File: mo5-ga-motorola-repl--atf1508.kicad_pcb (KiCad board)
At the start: 2 copper layers, 15 parts, among them J1 JTAG, J2 GATE_ARRAY_MO5_V1_SOCKET, J3 VPP, U1 ATF1508AS_L_100A_TQFP_JTAG_EN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

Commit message: pcb : adjusting
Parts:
- moved C8 30.0 mm to (132.5, 119.7)
- moved C1 6.98 mm to (97.5, 119.4), turned to 0 degrees
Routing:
- net GND: track 2.92 -> 21.1 mm, vias 0 -> 1
- net +5V: track 0.00 -> 2.43 mm, vias 0 -> 1
- net /CPLD/TDI: track 8.51 -> 7.91 mm
- added copper zone on B.Cu, net GND
- added copper zone on F.Cu, net GND
- added copper zone on In1.Cu, net GND
- added copper zone on In2.Cu, net GND
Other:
- copper layers 2 -> 4

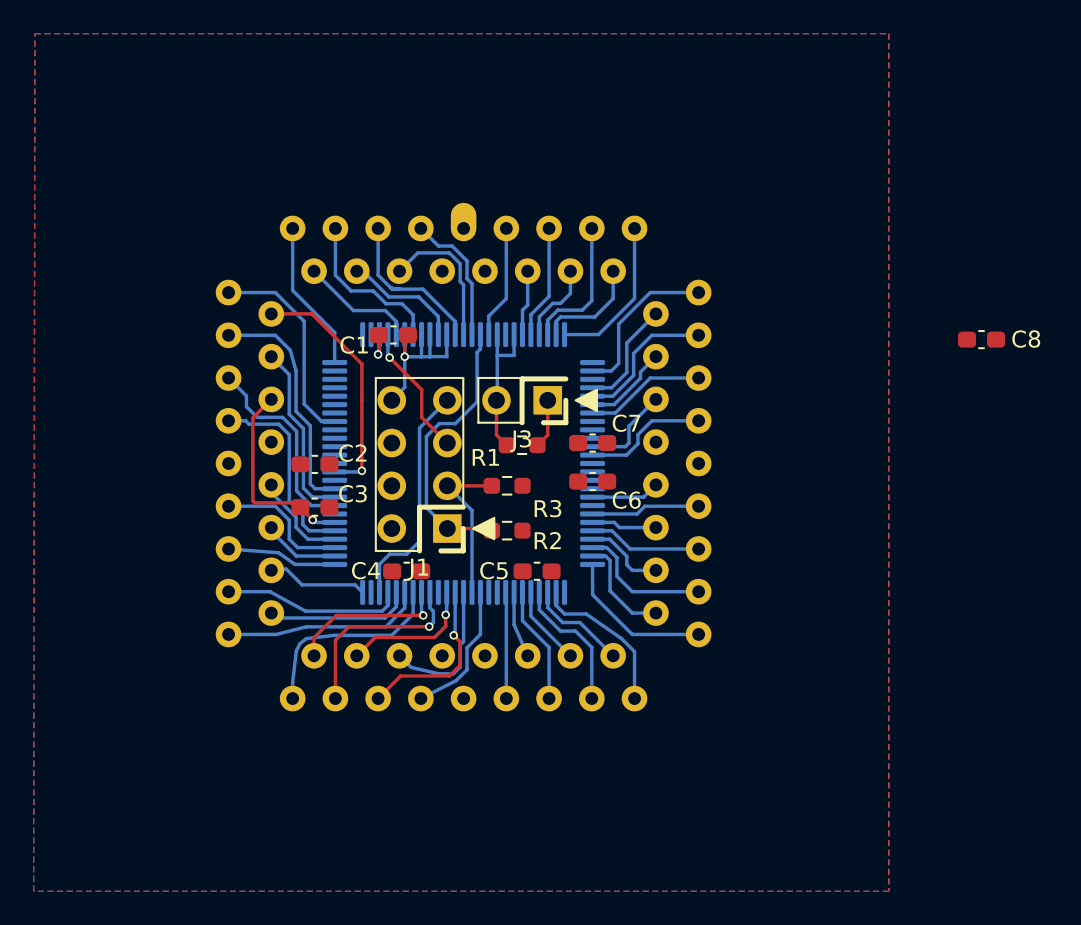
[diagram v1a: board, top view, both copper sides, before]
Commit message: pcb : slowly adjusting traces
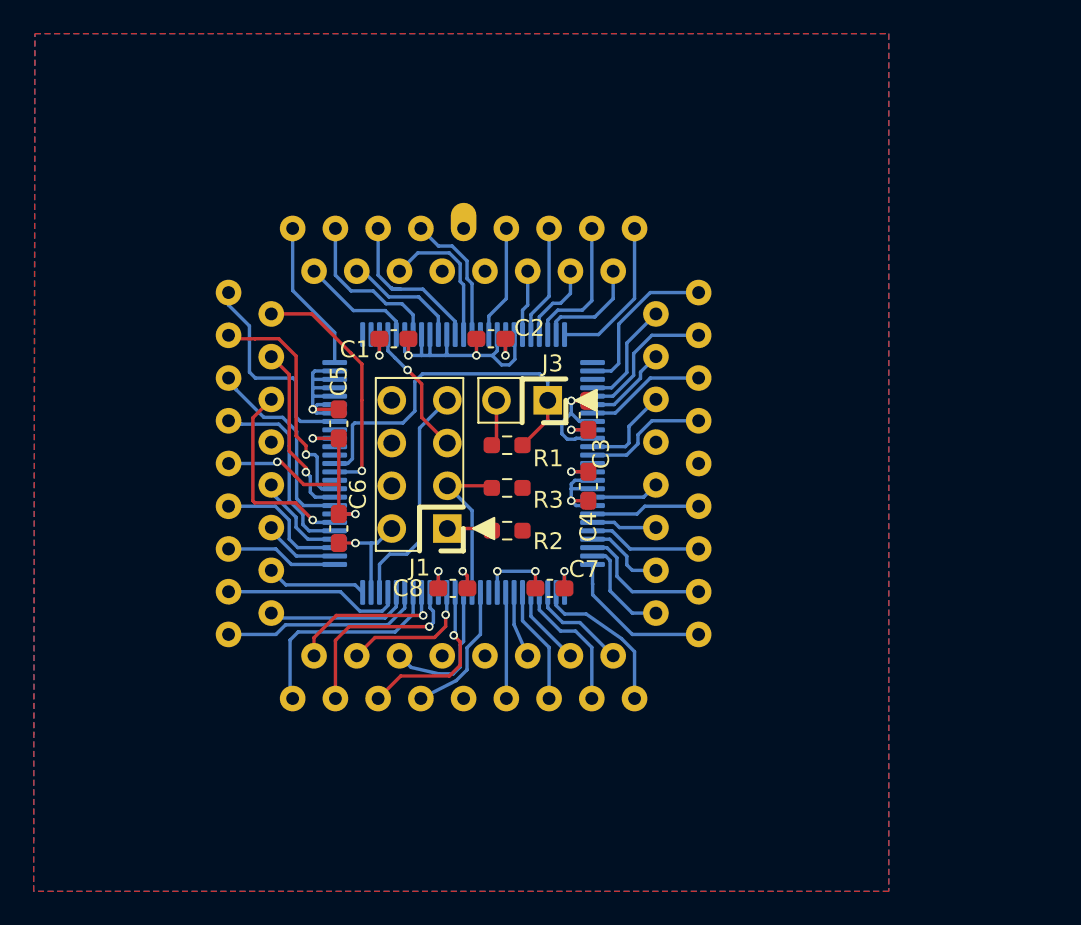
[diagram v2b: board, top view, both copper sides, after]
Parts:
- moved C8 34.7 mm to (101.0, 134.5), turned to 180 degrees
- moved C3 17.1 mm to (109.1, 124.2), turned to -90 degrees
- moved C6 15.3 mm to (94.3, 130.9), turned to -90 degrees
- moved C5 14.7 mm to (94.3, 124.7), turned to 90 degrees
- moved C2 12.9 mm to (103.3, 119.7)
- moved C4 11.9 mm to (109.1, 128.4), turned to 90 degrees
- moved C7 9.00 mm to (106.8, 134.5)
- moved R1 0.89 mm to (104.3, 126.0)
- moved C1 0.23 mm to (97.5, 119.7)
- moved R3 0.13 mm to (104.3, 128.5)
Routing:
- net GND: track 21.1 -> 56.3 mm, vias 1 -> 9
- net +5V: track 2.43 -> 30.3 mm, vias 1 -> 9
- net /CPLD/VPP: track 2.92 -> 21.7 mm
- net /CPLD/TMS: track 16.6 -> 2.70 mm
- net CLOCK: track 12.0 -> 12.8 mm
- net ~{CKLP}: track 13.9 -> 14.1 mm, vias 0 -> 1
- net SYCL: track 10.7 -> 10.6 mm, vias 0 -> 1

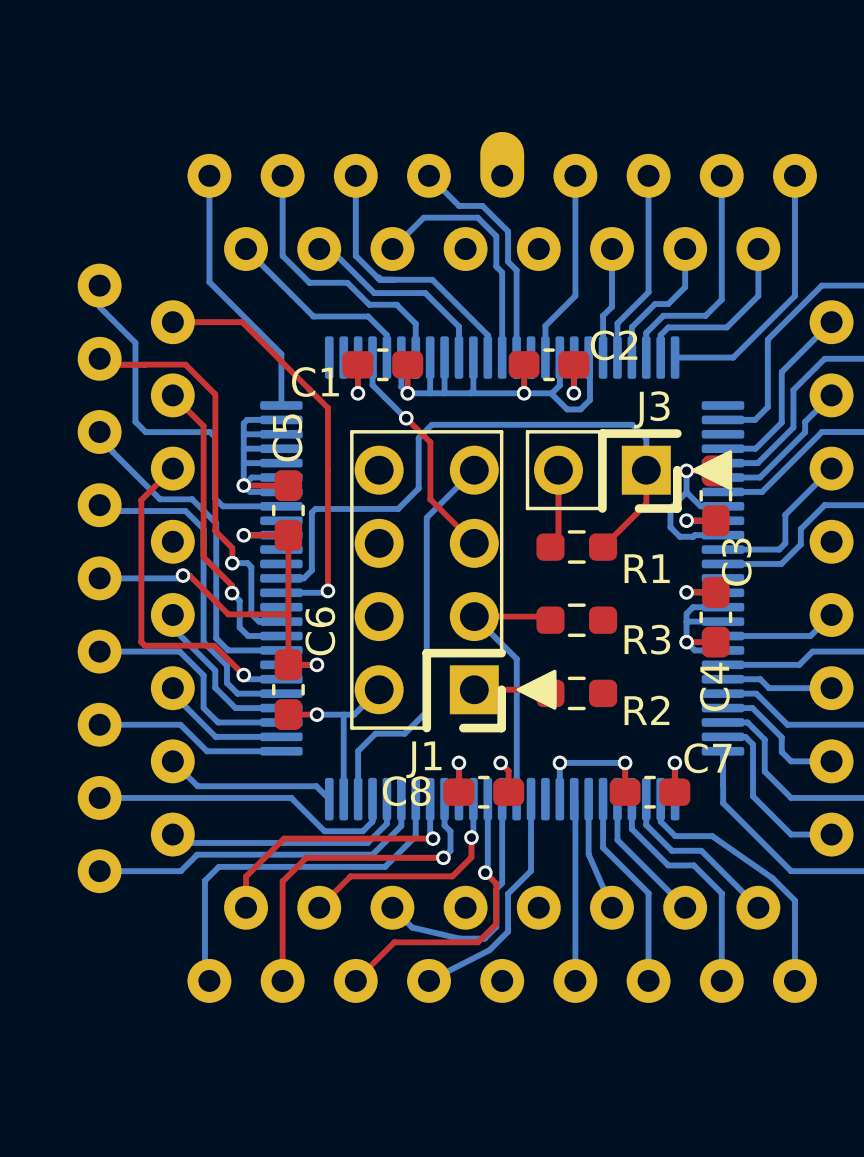
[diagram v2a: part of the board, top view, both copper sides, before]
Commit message: pcb : adjusting traces
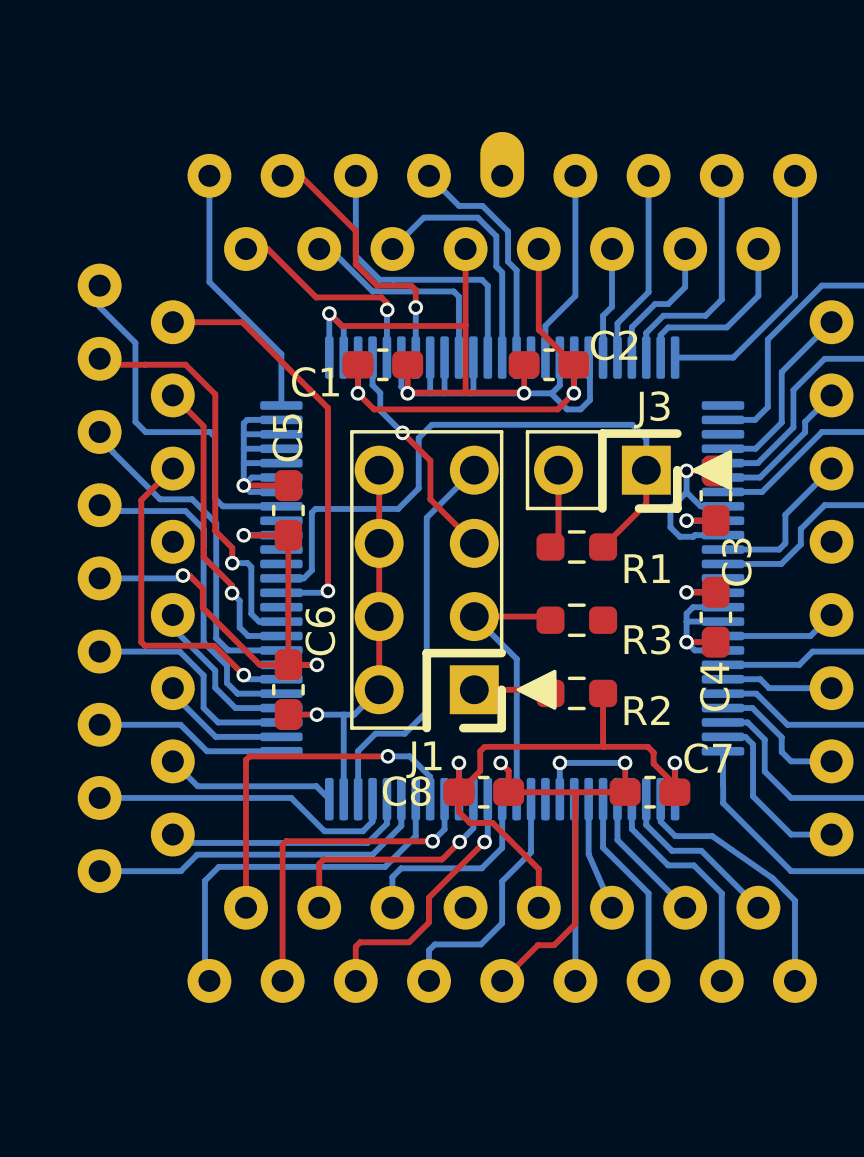
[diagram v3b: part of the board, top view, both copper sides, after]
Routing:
- net GND: track 56.3 -> 94.4 mm, vias 9 -> 10
- net +5V: track 30.3 -> 61.0 mm
- net Q: track 9.52 -> 12.6 mm
- net ITLP: track 8.62 -> 6.98 mm
- net ~{CAS_EXT}: track 10.2 -> 9.20 mm
- net ~{INITLT}: track 6.91 -> 7.57 mm, vias 0 -> 1
- net MADDR8: track 7.04 -> 7.65 mm
- net CT: track 8.19 -> 8.71 mm
- net A/SYNLT: track 9.55 -> 9.36 mm, vias 0 -> 1

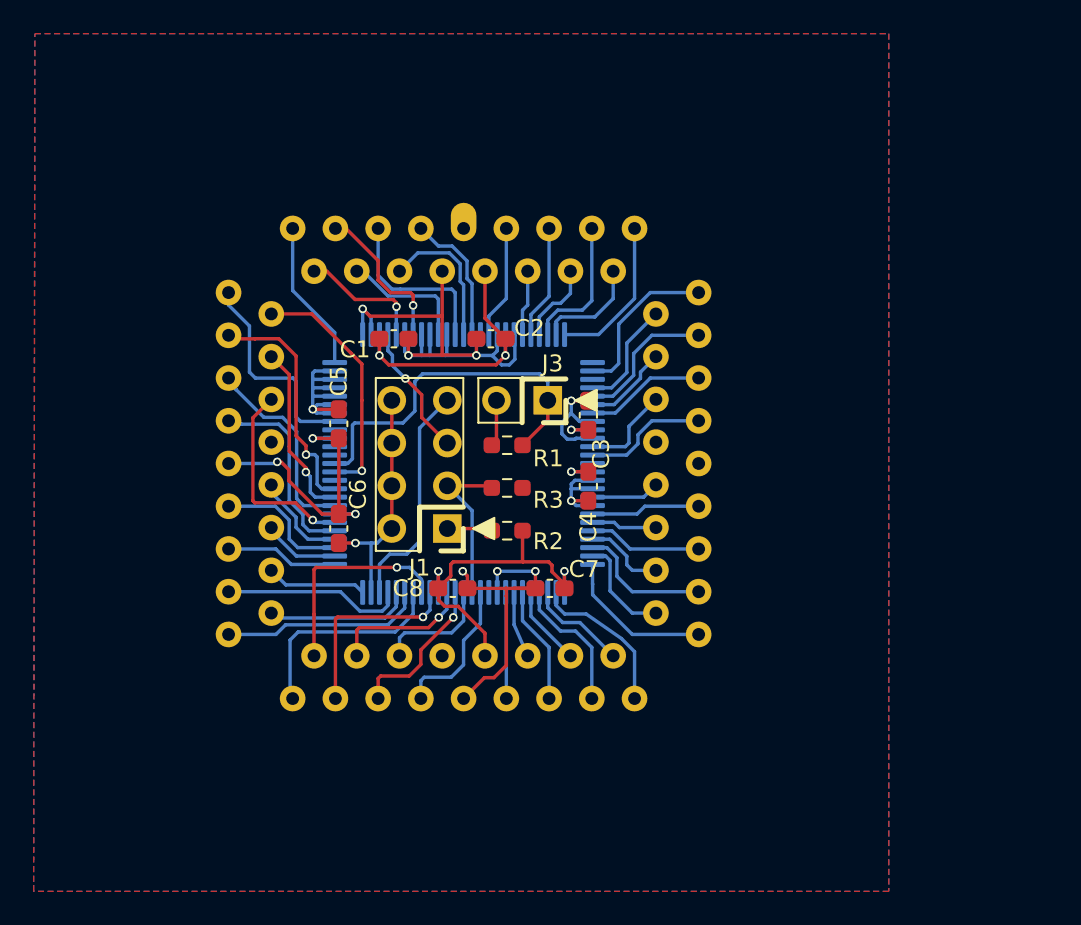
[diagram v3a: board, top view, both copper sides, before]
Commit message: pcb/schematics : rework connexion for easier routing, pcb edge, power distribution network
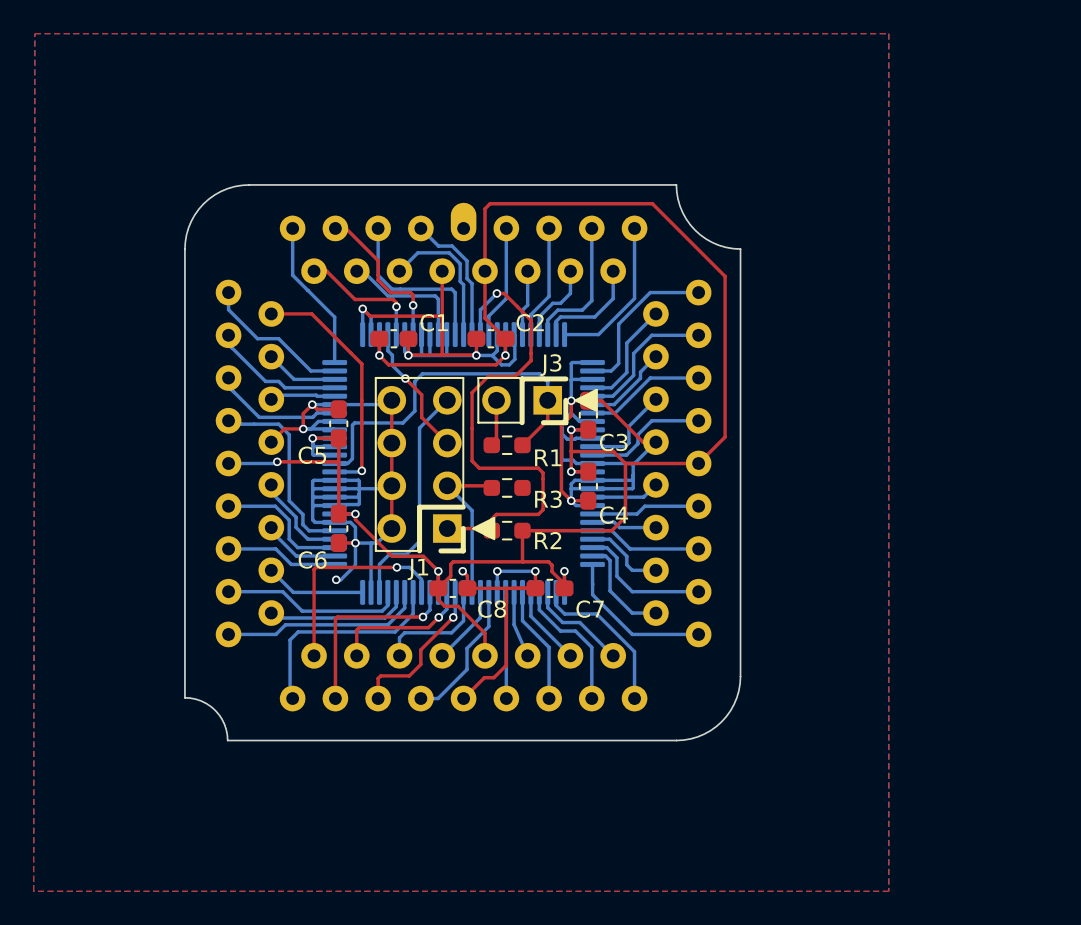
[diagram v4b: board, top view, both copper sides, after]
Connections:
- U1 pad 60: NC36 -> CT
- U1 pad 61: CT -> NC36
- U1 pad 81: ~{CS_PT} -> GND
- U1 pad 83: ~{CS_EXT} -> GND
- U1 pad 84: SYCL -> GND
- U1 pad 85: ~{CKLP} -> GND
- U1 pad 93: ~{POINT} -> GND
- U1 pad 94: GND -> ~{CS_EXT}
- U1 pad 96: GND -> ~{CS_PT}
- U1 pad 97: GND -> ~{CKLP}
- U1 pad 98: GND -> SYCL
- U1 pad 99: GND -> ~{POINT}
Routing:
- net +5V: track 61.0 -> 121.2 mm
- net GND: track 94.4 -> 151.4 mm, vias 10 -> 12
- net /CPLD/TMS: track 2.70 -> 29.6 mm, vias 0 -> 1
- net ~{CS_PT}: track 11.9 -> 3.90 mm, vias 1 -> 0
- net SYCL: track 10.6 -> 4.33 mm, vias 1 -> 0
- net ~{CKLP}: track 14.1 -> 8.23 mm, vias 1 -> 0
- net NC36: track 0.00 -> 4.71 mm
- net ~{CS_EXT}: track 11.9 -> 7.98 mm
- net ~{POINT}: track 12.8 -> 8.84 mm
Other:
- board outline added: 33 x 33 mm

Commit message: prepare release
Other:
- board text added: "face up"
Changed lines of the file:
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@@
   (title_block
     (title "Replacement of the Motorola gate array by ATF1508 CPLD")
-    (date "2025-05-24")
-    (rev "DRAFT-0")
+    (date "2025-07-13")
+    (rev "v1.0.0")
     (company "Sporniket")
     (comment 1 "For the 8-bits computer known as 'Thomson MO5' released in 1984")
@@
       (net 2 "GND") (pinfunction "GND") (pintype "passive"))
   )
+  (gr_circle (center 113.665 114.935) (end 114.935 114.935)
+    (stroke (width 0.1) (type solid)) (fill solid) (layer "F.SilkS"))
   (gr_line (start 85.117077 140.997077) (end 85.117077 114.327077)
     (stroke (width 0.1) (type default)) (layer "Edge.Cuts"))
@@
   (gr_line (start 118.137077 114.327077) (end 118.137077 139.727077)
     (stroke (width 0.1) (type default)) (layer "Edge.Cuts"))
+  (gr_text "face\nup" (at 86.995 112.395) (layer "F.SilkS")
+    (effects (font (size 1 1) (thickness 0.1)) (justify left top))
+  )
   (segment (start 94.2594 125.5776) (end 92.71 125.5776) (width 0.2032) (layer "F.Cu") (net 1))
   (segment (start 109.093 125.0696) (end 108.077 125.0696) (width 0.2032) (layer "F.Cu") (net 1))
